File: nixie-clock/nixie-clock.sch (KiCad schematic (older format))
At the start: 26 parts, among them Q1 2N7002, Q2 2N7002, Q3 2N7002, Q4 2N7002, Q5 2N7002, U1 ESP32-WROOM-32D, U2 HV5523, U3 HV5523

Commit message: Move keyboard stuff to it's own folder
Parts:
- added T?: NA5920-AL, symbol custom-parts:NA5920-AL
- added U?: DS3231M, Package_SO:SOIC-16W_7.5x10.3mm_P1.27mm, symbol Timer_RTC:DS3231M
- added U?: TPS40210, symbol custom-parts:TPS40210
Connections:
- net GND: now also U?.11 (GND), U?.6 (GND)
- net VDD: now also U?.10 (VDD)
- new net: U?.10 (GND), U?.11 (GND), U?.12 (GND), U?.13 (GND), U?.5 (GND), U?.6 (GND), U?.7 (GND), U?.8 (GND), U?.9 (GND)
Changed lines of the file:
@@
 Wire Wire Line
 	2300 4950 2300 5050
+$Comp
+L custom-parts:NA5920-AL T?
+U 1 1 5C300371
+P 5800 12350
+F 0 "T?" H 5800 12975 50  0000 C CNN
+F 1 "NA5920-AL" H 5800 12884 50  0000 C CNN
+F 2 "" H 5200 12850 50  0001 C CNN
+F 3 "" H 5200 12850 50  0001 C CNN
+	1    5800 12350
+	1    0    0    -1
+$EndComp
+$Comp
+L Timer_RTC:DS3231M U?
+U 1 1 5C31CD5B
+P 19850 1850
+F 0 "U?" H 19850 1364 50  0000 C CNN
+F 1 "DS3231M" H 19850 1273 50  0000 C CNN
+F 2 "Package_SO:SOIC-16W_7.5x10.3mm_P1.27mm" H 19850 1250 50  0001 C CNN
+F 3 "http://datasheets.maximintegrated.com/en/ds/DS3231.pdf" H 20120 1900 50  0001 C CNN
+	1    19850 1850
+	1    0    0    -1
+$EndComp
+$Comp
+L custom-parts:TPS40210 U?
+U 1 1 5C372B65
+P 2350 12300
+F 0 "U?" H 2450 12900 50  0000 C CNN
+F 1 "TPS40210" H 2600 12800 50  0000 C CNN
+F 2 "" H 2350 12150 50  0001 C CNN
+F 3 "" H 2350 12150 50  0001 C CNN
+	1    2350 12300
+	1    0    0    -1
+$EndComp
+$Comp
+L power:GND #PWR?
+U 1 1 5C37375D
+P 2350 12950
+F 0 "#PWR?" H 2350 12700 50  0001 C CNN
+F 1 "GND" H 2350 12800 50  0000 C CNN
+F 2 "" H 2350 12950 50  0001 C CNN
+F 3 "" H 2350 12950 50  0001 C CNN
+	1    2350 12950
+	1    0    0    -1
+$EndComp
+$Comp
+L power:VDD #PWR?
+U 1 1 5C373ED2
+P 2350 11650
+F 0 "#PWR?" H 2350 11500 50  0001 C CNN
+F 1 "VDD" H 2350 11800 50  0000 C CNN
+F 2 "" H 2350 11650 50  0001 C CNN
+F 3 "" H 2350 11650 50  0001 C CNN
+	1    2350 11650
+	1    0    0    -1
+$EndComp
+Wire Wire Line
+	2350 11650 2350 11750
+Wire Wire Line
+	2350 12850 2350 12950
 $EndSCHEMATC

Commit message: Nixie Clock progress
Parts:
- removed U?: TPS40210, symbol custom-parts:TPS40210
- added 0.015: R, symbol Device:R
- added C?: 250uF 4.7mOhm, symbol Device:C
- added C? (x2): 1uF, symbol Device:C
- added C?: 100pF 250V, symbol Device:C
- added C?: 2uF 250V 67mOhm, symbol Device:C
- added C?: 200nF, symbol Device:C
- added C?: 470pF, symbol Device:C
- added C?: 5.5nF, symbol Device:C
- added C?: 7.4pF, symbol Device:C
- added C?: C, symbol pspice:C
- added C?: 230pF, symbol Device:C
- added D?: RFN2LAM6STFTR, symbol custom-parts:RFN2LAM6STFTR
- added Q?: PSMN014-80YL, Package_TO_SOT_SMD:LFPAK56, symbol custom-parts:PSMN014-80YL
- added R?: 400k, symbol Device:R
- added R?: 0, symbol Device:R
- added R?: 240k, symbol Device:R
- added R? (x2): 1k, symbol Device:R
- added R?: 28k, symbol Device:R
- added U?: TPS40210, Package_SO:MSOP-10-1EP_3x3mm_P0.5mm_EP1.68x1.88mm, symbol custom-parts:TPS40210
- T?: symbol custom-parts:NA5920-AL -> nixie-clock-rescue:NA5920-AL-custom-parts
- U2, U3: symbol custom-parts:HV5523 -> nixie-clock-rescue:HV5523-custom-parts
- U? (x2): symbol custom-parts:LDL1117 -> nixie-clock-rescue:LDL1117-custom-parts
- V? (x6): symbol custom-parts:IN-18 -> nixie-clock-rescue:IN-18-custom-parts
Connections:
- net labels added: HVDIS
- wire segments 318 -> 402

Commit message: Add seprate project for HV supply validation
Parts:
- added R? (x6): 3.3k, symbol Device:R
- T?: symbol nixie-clock-rescue:NA5920-AL-custom-parts -> custom-parts:NA5920-AL
- U2, U3: symbol nixie-clock-rescue:HV5523-custom-parts -> custom-parts:HV5523
- U? (x2): symbol nixie-clock-rescue:LDL1117-custom-parts -> custom-parts:LDL1117
- V? (x6): symbol nixie-clock-rescue:IN-18-custom-parts -> custom-parts:IN-18
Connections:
- net labels added: RTC_INT, RTC_RST, RTC_SCL, RTC_SDA, RTL_RST, RTL_SDA
- wire segments 402 -> 427
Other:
- moved on the sheet: 0.015, C?, D?, Q?, R?, U?

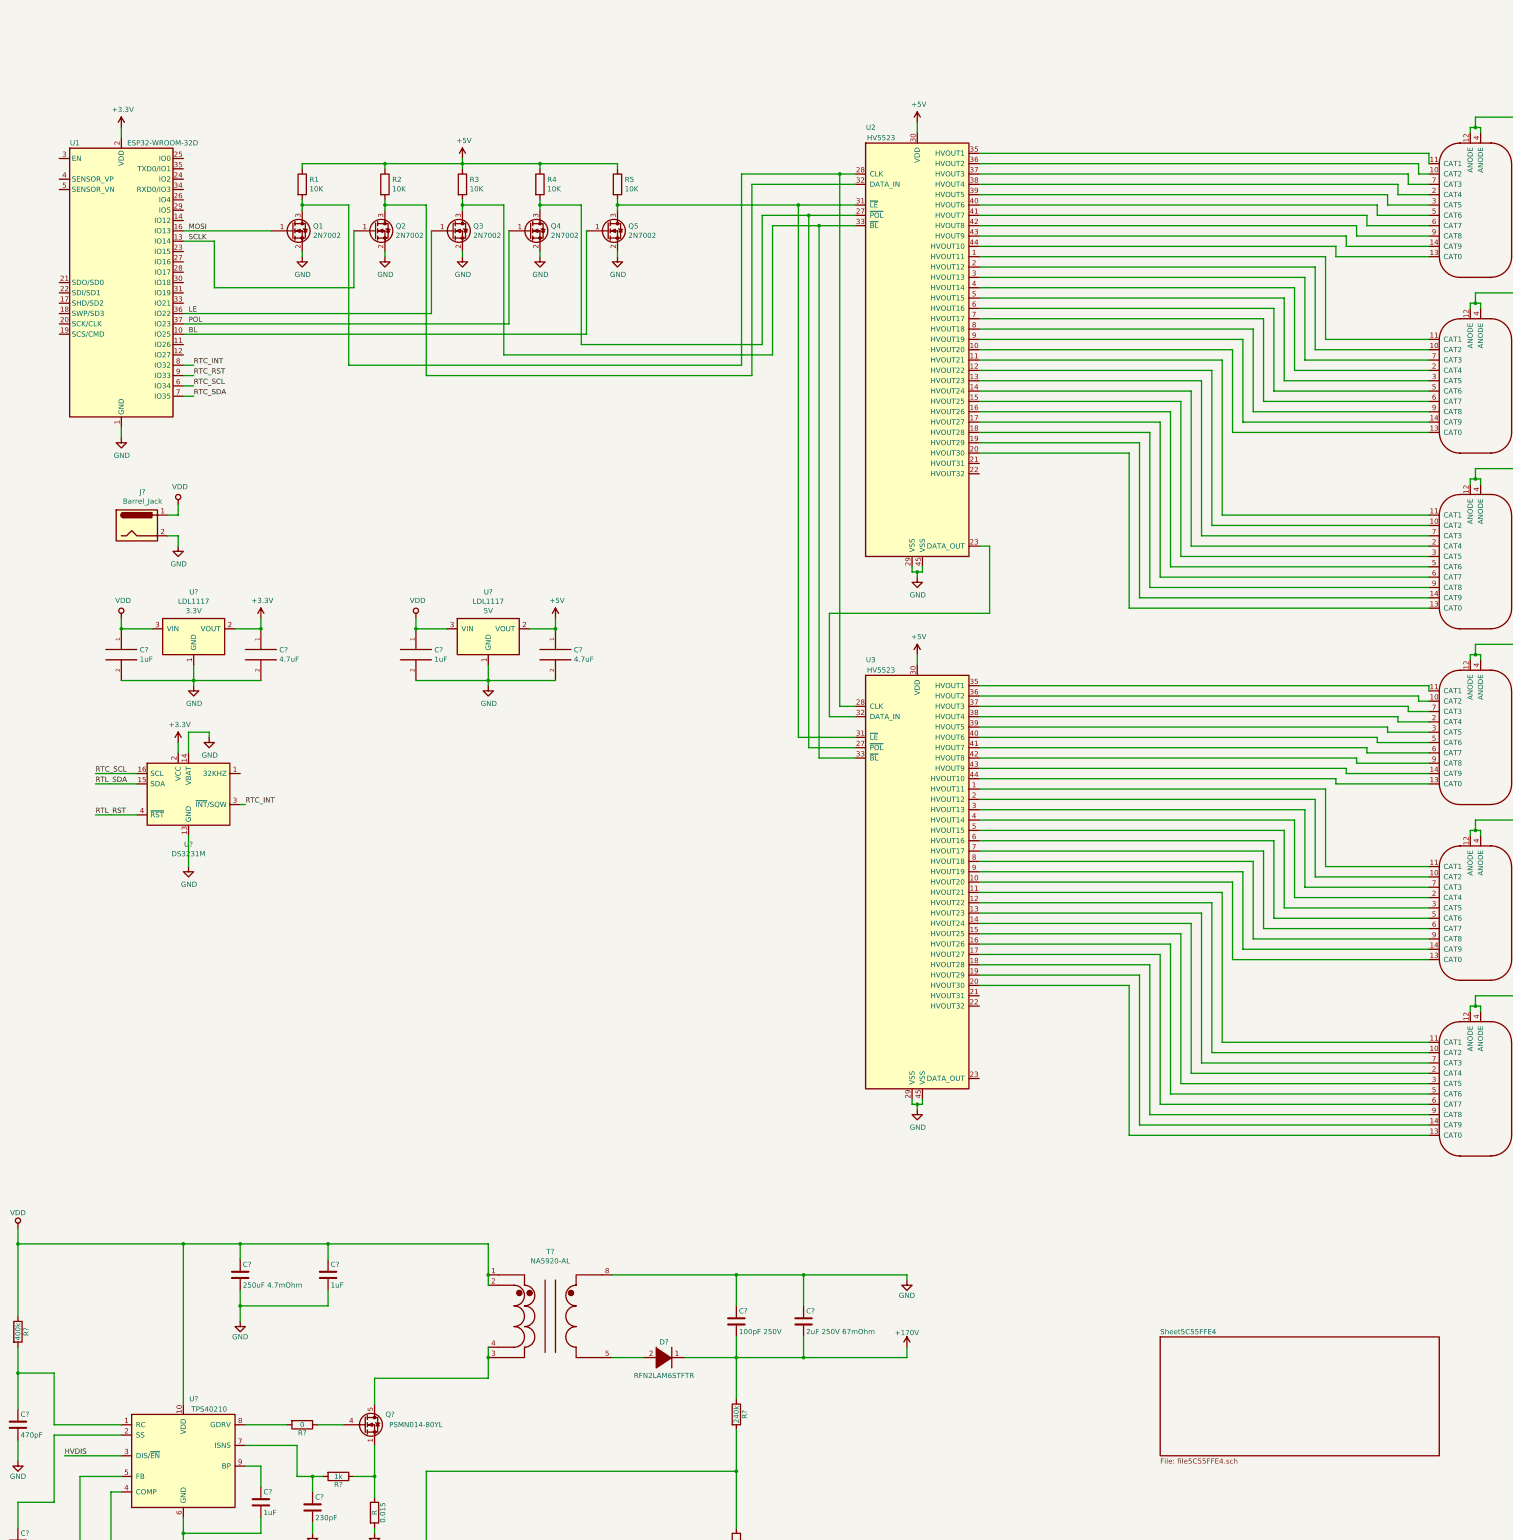
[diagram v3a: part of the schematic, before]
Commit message: Clock schematic draft finished
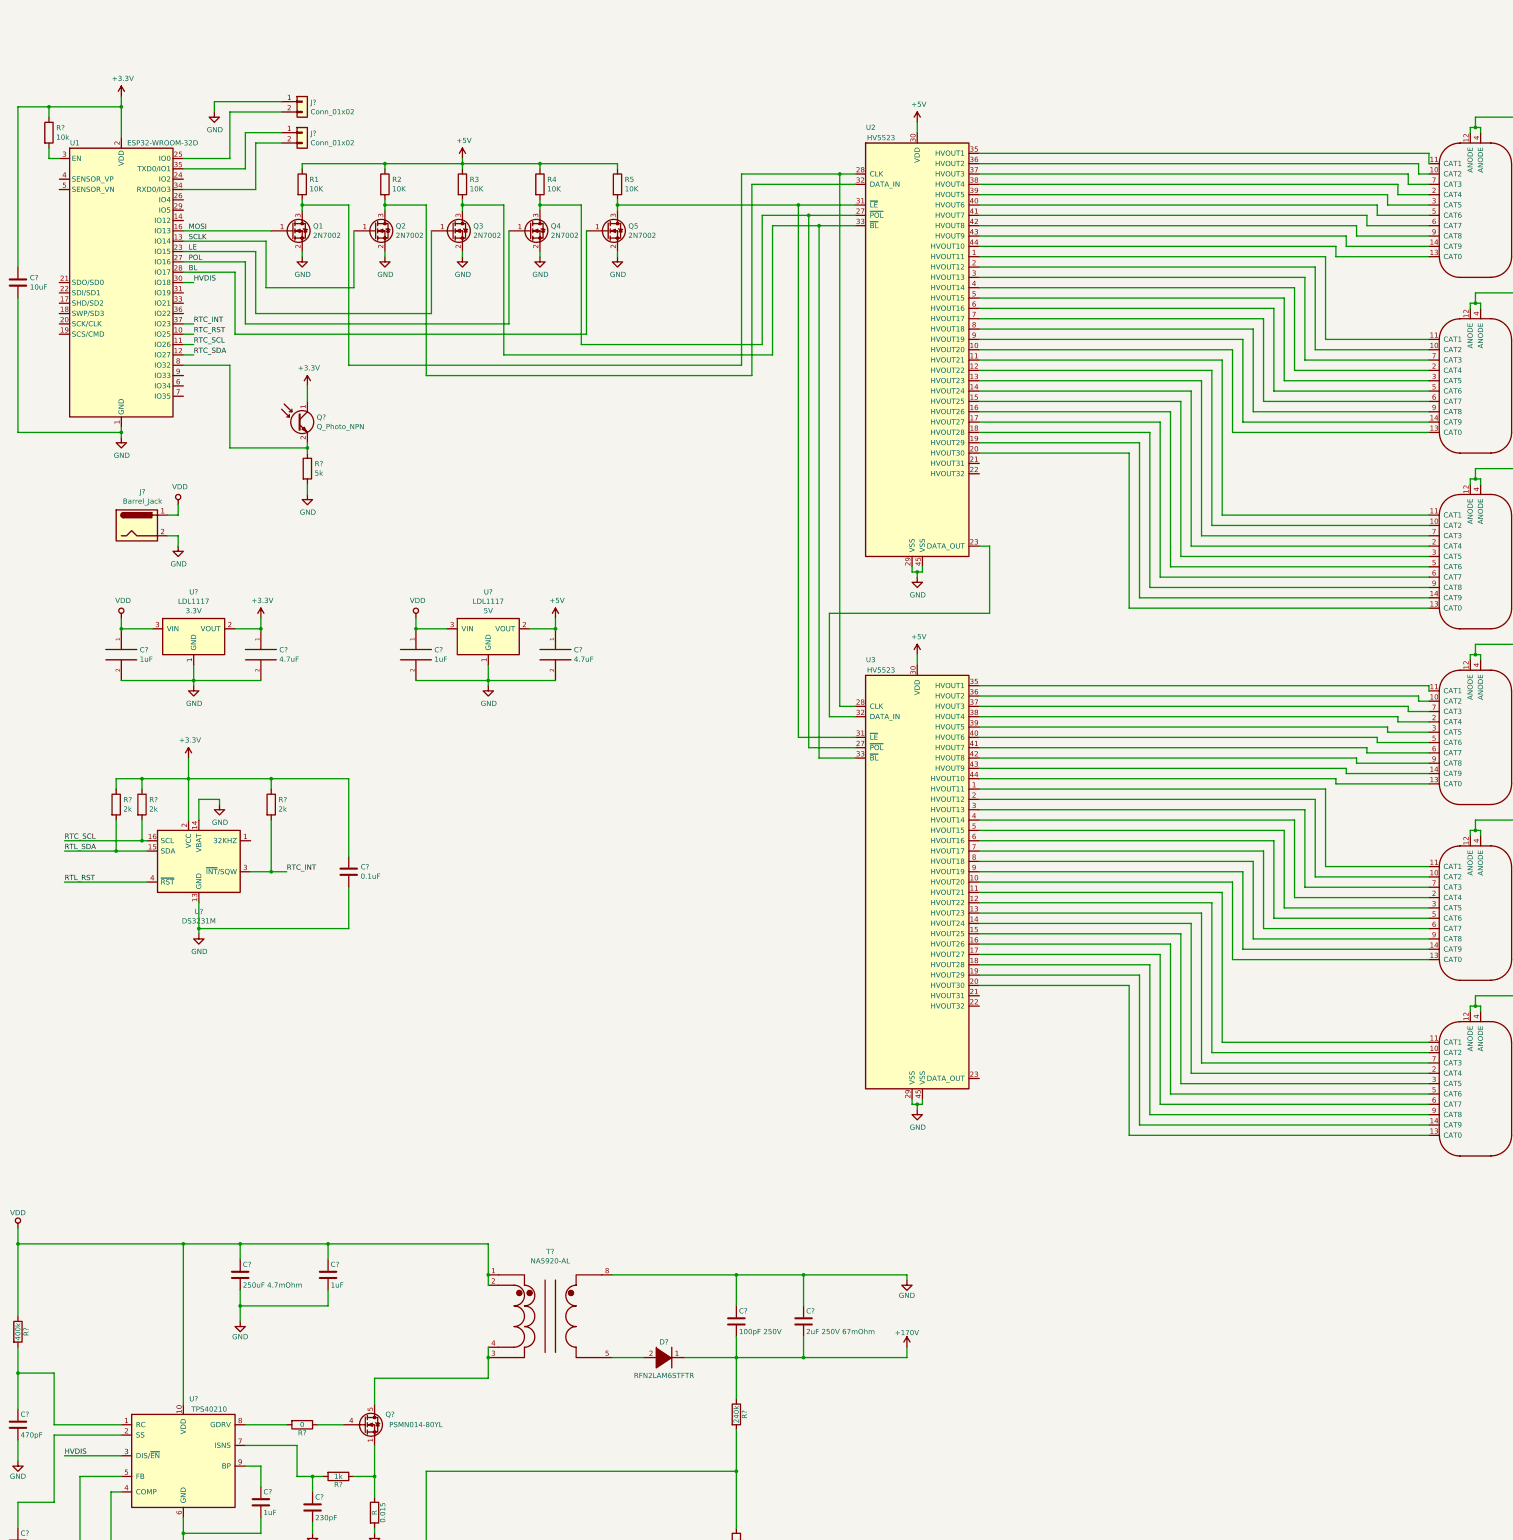
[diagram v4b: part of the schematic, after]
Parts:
- added C?: 10uF, symbol Device:C
- added C?: 0.1uF, symbol Device:C
- added J? (x2): Conn_01x02, symbol Connector_Generic:Conn_01x02
- added Q?: Q_Photo_NPN, Resistor_SMD:R_1206_3216Metric_Pad1.42x1.75mm_HandSolder, symbol Device:Q_Photo_NPN
- added R?: 5k, symbol Device:R
- added R?: 10k, symbol Device:R
- added R? (x3): 2k, symbol Device:R
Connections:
- net +3V3: now also C?.1, C?.1, Q?.1 (C), R?.1, R?.1, R?.1, R?.1
- net BL: now also U1.28 (IO17); no longer U1.10 (IO25)
- net GND: now also C?.2, C?.2, J?.1 (Pin_1), R?.2
- net HVDIS: now also U1.30 (IO18)
- net LE: now also U1.23 (IO15); no longer U1.36 (IO22)
- net POL: now also U1.27 (IO16); no longer U1.37 (IO23)
- net RTC_INT: now also U1.37 (IO23), R?.2; no longer U1.8 (IO32)
- net RTC_RST: now also U1.10 (IO25); no longer U1.9 (IO33)
- net RTC_SCL: now also U1.11 (IO26), R?.2; no longer U1.6 (IO34)
- net RTC_SDA: now also U1.12 (IO27); no longer U1.7 (IO35)
- net RTL_SDA: now also R?.2
- net at U1.25 (IO0): now also J?.2 (Pin_2)
- net at U1.3 (EN): now also R?.2
- net at U1.34 (RXD0/IO3): now also J?.2 (Pin_2)
- net at U1.35 (TXD0/IO1): now also J?.1 (Pin_1)
- new net: Q?.2 (E), R?.1, U1.8 (IO32)
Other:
- moved on the sheet: U?

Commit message: Preliminary / rough board layout
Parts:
- removed C?: C, symbol pspice:C
- added C18, C19, C7: 0.1uF, Capacitor_SMD:C_0805_2012Metric_Pad1.15x1.40mm_HandSolder, symbol Device:C
- added D1: D_Zener, Diode_SMD:D_SOD-123, symbol Device:D_Zener
- added D2: D_Schottky, Diode_SMD:D_1206_3216Metric_Castellated, symbol Device:D_Schottky
- C1, C10, C11, C12, C13, C14, C15, C16, C2, C3, C4, C5, C6, C9: renamed from C?; footprint (none) -> Capacitor_SMD:C_0805_2012Metric_Pad1.15x1.40mm_HandSolder
- C17: renamed from C?; footprint (none) -> Capacitor_SMD:C_2220_5650Metric_Pad1.97x5.40mm_HandSolder
- C8: renamed from C?; value 250uF 4.7mOhm -> 220uF 25mOhm; footprint (none) -> Capacitor_SMD:C_2816_7142Metric_Pad3.20x4.45mm_HandSolder; Part Number (none) -> TPME227K016R0025
- D3: renamed from D?; footprint (none) -> custom-parts:SOD-128-2
- J1: renamed from J?; footprint (none) -> Connector_BarrelJack:BarrelJack_CUI_PJ-102AH_Horizontal
- J2, J3: renamed from J?; footprint (none) -> Connector_PinHeader_1.00mm:PinHeader_1x02_P1.00mm_Vertical
- R1, R2, R3, R4, R5: footprint (none) -> Resistor_SMD:R_0805_2012Metric_Pad1.15x1.40mm_HandSolder
- R10, R11, R12, R16, R17, R18, R19, R20, R21, R22, R23, R6, R7, R8, R9: renamed from R?; footprint (none) -> Resistor_SMD:R_0805_2012Metric_Pad1.15x1.40mm_HandSolder
- R13, R14: renamed from R?; footprint (none) -> Capacitor_SMD:C_0805_2012Metric_Pad1.15x1.40mm_HandSolder
- R15: renamed from 0.015; value R -> 0.015; footprint (none) -> custom-parts:R_GMR_100
- T1: renamed from T?; footprint (none) -> custom-parts:NA6252-AL
- U2: footprint (none) -> Package_DFN_QFN:QFN-44-1EP_7x7mm_P0.5mm_EP5.15x5.15mm
- U5, U7: renamed from U?; footprint (none) -> Package_TO_SOT_SMD:SOT-223-3_TabPin2
- V1, V2, V3, V4, V5, V6: renamed from V?; footprint (none) -> custom-parts:IN-18 Socket
- gave numbers to parts that had none: 4
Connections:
- net +5V: now also C18.1, C19.1
- net GND: now also C18.2, C19.2, C7.2
- net VDD: now also D1.2 (A)
- net at Q6.2 (E), R13.1, U1.8 (IO32): now also C7.1
- net at Q7.5 (D), T1.3, T1.4: now also D2.2 (A)
- new net: D1.1 (K), D2.1 (K)
